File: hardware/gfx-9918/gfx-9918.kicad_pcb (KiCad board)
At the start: 2 copper layers, 50 x 150 mm, 28 parts, among them J1 GFX_Connector_Input, J2 AV, J3 Sound L, J4 Sound R, U1 TMS9918, U2 74HCT04, U3 74HCT574, U4 74HCT574, U5 74HCT574, U6 HM62256ALP-10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

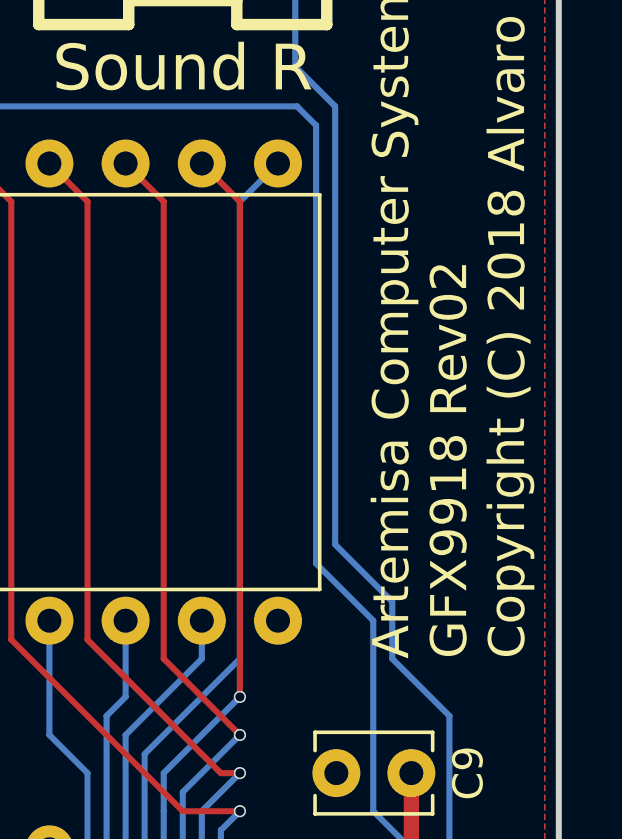
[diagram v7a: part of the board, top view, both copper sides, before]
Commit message: [gfx9918] Bump to rev 3
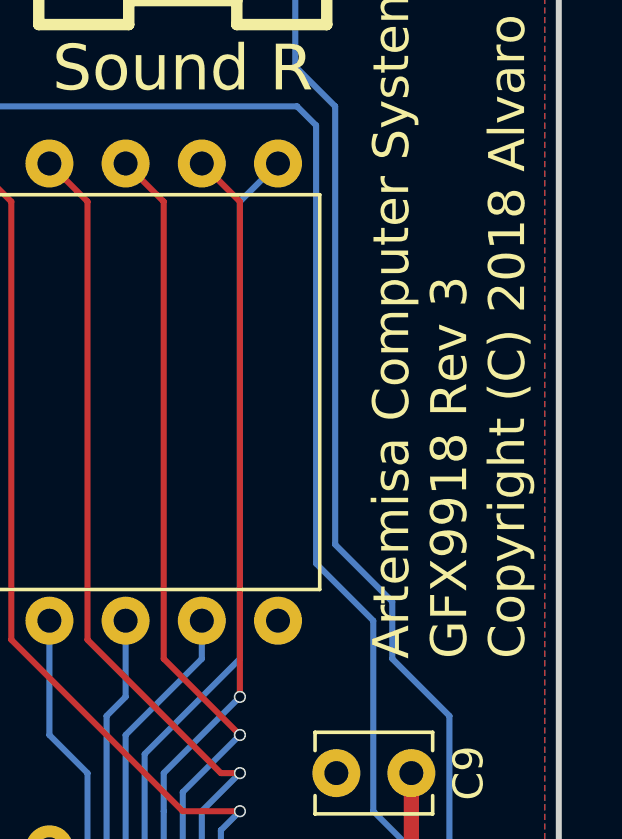
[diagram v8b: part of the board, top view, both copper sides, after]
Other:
- board text added: "Artemisa Computer System GFX9918 Rev 3 Copyright (C) 2018 Alvaro Polo"
- board text removed: "Artemisa Computer System GFX9918 Rev02 Copyright (C) 2018 Alvaro Polo"
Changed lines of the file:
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@@
       (xy -5.472572 -2.546406)) (layer F.SilkS) (width 0.01))
   )
-  (gr_text "Artemisa Computer System\nGFX9918 Rev02\nCopyright (C) 2018 Alvaro Polo" (at 90.355 80.05 90) (layer F.SilkS)
+  (gr_text "Artemisa Computer System\nGFX9918 Rev 3\nCopyright (C) 2018 Alvaro Polo" (at 90.355 80.05 90) (layer F.SilkS)
     (effects (font (size 1.2 1.2) (thickness 0.2)) (justify left))
   )
